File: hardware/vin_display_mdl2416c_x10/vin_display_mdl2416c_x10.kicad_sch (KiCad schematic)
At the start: 52 parts, among them J1 DEBUG, J2 USB_B_Micro, J3 DEBUG_UART, J4 Conn_01x04, J5 AUX_CONNECTOR, Q1 BSS138, SW1 SW_RESET, SW2 BOOTSEL, SW3 KNOB, U1 W25Q16JVSNIQ, U2 MIC23050-SYML, U3 RP2040, U4 HEF4028BT, X1 12MHz

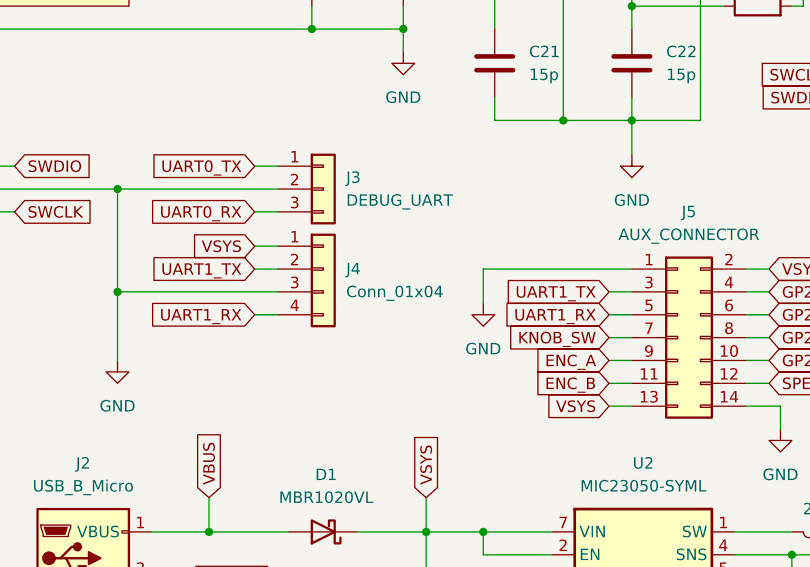
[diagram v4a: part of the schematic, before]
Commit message: mdl2416c_x10 pcb fixes/adjustments
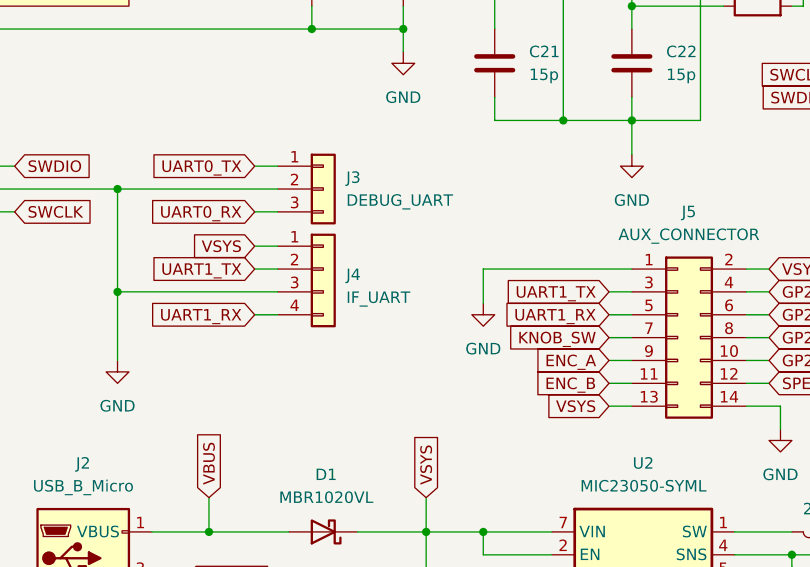
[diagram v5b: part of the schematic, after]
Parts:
- J4: value Conn_01x04 -> IF_UART
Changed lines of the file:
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@@
   (symbol (lib_id "Connector_Generic:Conn_01x04") (at 68.58 137.16 0) (unit 1)
     (in_bom yes) (on_board yes) (dnp no) (fields_autoplaced)
-    (property "Reference" "J4" (at 71.12 137.1599 0)
+    (property "Reference" "J4" (at 71.12 137.795 0)
       (effects (font (size 1.27 1.27)) (justify left))
     )
-    (property "Value" "Conn_01x04" (at 71.12 139.6999 0)
+    (property "Value" "IF_UART" (at 71.12 140.335 0)
       (effects (font (size 1.27 1.27)) (justify left))
     )

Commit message: minor schematic fixes
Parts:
- C21, C22: value 15p -> 19p
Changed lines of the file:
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@@
       (effects (font (size 1.27 1.27)) (justify left))
     )
-    (property "Value" "15p" (at 91.44 115.5699 0)
+    (property "Value" "19p" (at 91.44 115.5699 0)
       (effects (font (size 1.27 1.27)) (justify left))
     )
@@
       (effects (font (size 1.27 1.27)) (justify left))
     )
-    (property "Value" "15p" (at 106.68 115.5699 0)
-      (effects (font (size 1.27 1.27)) (justify left))
-    )
+    (property "Value" "19p" (at 106.68 115.5699 0)
+      (effects (font (size 1.27 1.27)) (justify left))
+    )

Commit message: update schematic; add pdf
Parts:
- removed U4: HEF4028BT, components:SO16, symbol components:HEF4028BT
- added U4: SN74HC42D, components:SO16, symbol components:SN74HC42D
- R10: value 10K -> 1K
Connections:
- net 3V3: now also U4.16 (VCC); no longer R10.2
- net DISP10_CE: now also U4.11 (9)
- net DISP1_CE: now also U4.1 (0)
- net DISP2_CE: now also U4.2 (1)
- net DISP3_CE: now also U4.3 (2)
- net DISP4_CE: now also U4.4 (3)
- net DISP5_CE: now also U4.5 (4)
- net DISP6_CE: now also U4.6 (5)
- net DISP7_CE: now also U4.7 (6)
- net DISP8_CE: now also U4.9 (7)
- net DISP9_CE: now also U4.10 (8)
- net DISP_CE_A0: now also U4.15 (A)
- net DISP_CE_A1: now also U4.14 (B)
- net DISP_CE_A2: now also U4.13 (C)
- net DISP_CE_A3: now also U4.12 (D)
- net GND: now also U4.8 (GND)
- net KNOB_SW: now also R10.2
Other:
- moved on the sheet: R10
